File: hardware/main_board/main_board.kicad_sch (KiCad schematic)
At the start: 98 parts, among them J1 USB_C_Receptacle_USB2.0_16P, J2 BAT1, J3 Conn_02x05_Odd_Even, J4 Conn_02x05_Odd_Even, Q1 FDMC4435BZ, Q2 MMBT3904, Q3 MMBT3904, SW1 PTS645VK31LFS, SW2 PTS645VK31LFS, SW3 PTS645VK31LFS, U1 SRV05-4, U10 TPS61022, U11 ESP32-S3-WROOM1, U12 TPS2121, U13 TPS22810DBVR, U2 CP2102N-A02-GQFN28, U3 HUSB238_002DD, U4 TPS22918DBVR, U5 BQ25601, U6 DFPlayer_mini, U7 DS3231MZ, U8 TPS63802, U9 NCH2800HV

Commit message: WIP: mainboard pcb layout
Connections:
- net GND: no longer C3.2
- net PGND1: now also C3.2
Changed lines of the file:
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@@
 	)
 	(symbol
+		(lib_id "power:GNDPWR")
+		(at 80.01 39.37 0)
+		(unit 1)
+		(exclude_from_sim no)
+		(in_bom yes)
+		(on_board yes)
+		(dnp no)
+		(fields_autoplaced yes)
+		(property "Reference" "#PWR014"
+			(at 80.01 44.45 0)
+			(effects
+				(font
+					(size 1.27 1.27)
+				)
+				(hide yes)
+			)
+		)
+		(property "Value" "PGND1"
+			(at 79.883 43.18 0)
+			(effects
+				(font
+					(size 1.27 1.27)
+				)
+			)
+		)
+		(property "Footprint" ""
+			(at 80.01 40.64 0)
+			(effects
+				(font
+					(size 1.27 1.27)
+				)
+				(hide yes)
+			)
+		)
+		(property "Datasheet" ""
+			(at 80.01 40.64 0)
+			(effects
+				(font
+					(size 1.27 1.27)
+				)
+				(hide yes)
+			)
+		)
+		(property "Description" "Power symbol creates a global label with name \"GNDPWR\" , global ground"
+			(at 80.01 39.37 0)
+			(effects
+				(font
+					(size 1.27 1.27)
+				)
+				(hide yes)
+			)
+		)
+		(pin "1"
+		)
+		(instances
+			(project "main_board"
+				(path "/62950e93-3f98-4dee-9256-8213caa98ee7"
+					(reference "#PWR014")
+					(unit 1)
+				)
+			)
+		)
+	)
+	(symbol
 		(lib_id "Johnson_Symbol_Lib:TPS22918DBVR")
 		(at 128.27 226.06 0)
@@
 					(unit 1)
 				)
-			)
-		)
-	)
-	(symbol
-		(lib_id "power:GND")
-		(at 80.01 39.37 0)
-		(unit 1)
-		(exclude_from_sim no)
-		(in_bom yes)
-		(on_board yes)
-		(dnp no)
-		(fields_autoplaced yes)
-		(property "Reference" "#PWR014"
-			(at 80.01 45.72 0)
-			(effects
-				(font
-					(size 1.27 1.27)
-				)
-				(hide yes)
-			)
-		)
-		(property "Value" "GND"
-			(at 80.01 44.45 0)
-			(effects
-				(font
-					(size 1.27 1.27)
-				)
-			)
-		)
-		(property "Footprint" ""
-			(at 80.01 39.37 0)
-			(effects
-				(font
-					(size 1.27 1.27)
-				)
-				(hide yes)
-			)
-		)
-		(property "Datasheet" ""
-			(at 80.01 39.37 0)
-			(effects
-				(font
-					(size 1.27 1.27)
-				)
-				(hide yes)
-			)
-		)
-		(property "Description" "Power symbol creates a global label with name \"GND\" , ground"
-			(at 80.01 39.37 0)
-			(effects
-				(font
-					(size 1.27 1.27)
-				)
-				(hide yes)
-			)
-		)
-		(pin "1"
-		)
-		(instances
-			(project "main_board"
-				(path "/62950e93-3f98-4dee-9256-8213caa98ee7"
-					(reference "#PWR014")
-					(unit 1)
-				)

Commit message: WIP: update mainboard componemt LCSC PN
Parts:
- C16: LCSC PN (none) -> C23692981
- J2: footprint Connector_JST:JST_XH_S2B-XH-A_1x02_P2.50mm_Horizontal -> Connector_JST:JST_PH_B2B-PH-SM4-TB_1x02-1MP_P2.00mm_Vertical; LCSC PN C240819 -> C3029431
- LS1: footprint Connector_JST:JST_XH_S2B-XH-A_1x02_P2.50mm_Horizontal -> Connector_JST:JST_PH_B2B-PH-SM4-TB_1x02-1MP_P2.00mm_Vertical; LCSC PN C19270574 -> (none)
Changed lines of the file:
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@@
 			)
 		)
-		(property "Footprint" "Connector_JST:JST_XH_S2B-XH-A_1x02_P2.50mm_Horizontal"
+		(property "Footprint" "Connector_JST:JST_PH_B2B-PH-SM4-TB_1x02-1MP_P2.00mm_Vertical"
 			(at 144.78 237.49 0)
 			(effects
@@
 			)
 		)
-		(property "LCSC PN" "C19270574"
+		(property "LCSC PN" ""
 			(at 144.78 242.57 0)
 			(effects
@@
 			)
 		)
-		(property "Footprint" "Connector_JST:JST_XH_S2B-XH-A_1x02_P2.50mm_Horizontal"
+		(property "Footprint" "Connector_JST:JST_PH_B2B-PH-SM4-TB_1x02-1MP_P2.00mm_Vertical"
 			(at 167.64 88.9 0)
 			(effects
@@
 			)
 		)
-		(property "LCSC PN" "C240819"
+		(property "LCSC PN" "C3029431"
 			(at 167.64 88.9 0)
 			(effects
@@
 			(at 274.32 43.18 0)
 			(effects
+				(font
+					(size 1.27 1.27)
+				)
+				(hide yes)
+			)
+		)
+		(property "LCSC PN" "C23692981"
+			(at 274.32 43.18 0)
+			(effects

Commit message: WIP: update component LCSCPN
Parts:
- J2, LS1: now in the parts list
- R29: LCSC PN (none) -> C102991
- R7: LCSC PN (none) -> C25077
- R73: LCSC PN (none) -> C21189
- U10: LCSC PN (none) -> C2071784
- U8: LCSC PN (none) -> C2845237
- U9: now left out of the parts list
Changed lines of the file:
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@@
 			)
 		)
-		(property "LCSC PN" ""
+		(property "LCSC PN" "C21189"
 			(at 256.54 201.93 90)
 			(effects
@@
 		(unit 1)
 		(exclude_from_sim no)
-		(in_bom yes)
+		(in_bom no)
 		(on_board yes)
 		(dnp no)
@@
 		(unit 1)
 		(exclude_from_sim no)
-		(in_bom no)
+		(in_bom yes)
 		(on_board yes)
 		(dnp no)
@@
 		(unit 1)
 		(exclude_from_sim no)
-		(in_bom no)
+		(in_bom yes)
 		(on_board yes)
 		(dnp no)
@@
 			)
 		)
+		(property "LCSC PN" "C2845237"
+			(at 245.11 41.91 0)
+			(effects
+				(font
+					(size 1.27 1.27)
+				)
+				(hide yes)
+			)
+		)
 		(pin "9"
 		)
@@
 			)
 		)
+		(property "LCSC PN" "C2071784"
+			(at 278.13 80.01 0)
+			(effects
+				(font
+					(size 1.27 1.27)
+				)
+				(hide yes)
+			)
+		)
 		(pin "4"
 		)
@@
 			)
 		)
+		(property "LCSC PN" "C102991"
+			(at 309.88 25.4 0)
+			(effects
+				(font
+					(size 1.27 1.27)
+				)
+				(hide yes)
+			)
+		)
 		(pin "1"
 		)
@@
 			)
 		)
-		(property "LCSC PN" ""
+		(property "LCSC PN" "C25077"
 			(at 111.76 38.1 90)
 			(effects

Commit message: WIP: mainboard schematic
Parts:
- R18: LCSC PN C11616 -> C100463
- SW1, SW2, SW3: now left out of the parts list
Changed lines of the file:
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@@
 		(unit 1)
 		(exclude_from_sim no)
-		(in_bom yes)
+		(in_bom no)
 		(on_board yes)
 		(dnp no)
@@
 		(unit 1)
 		(exclude_from_sim no)
-		(in_bom yes)
+		(in_bom no)
 		(on_board yes)
 		(dnp no)
@@
 			)
 		)
-		(property "LCSC PN" "C11616"
+		(property "LCSC PN" "C100463"
 			(at 265.43 38.1 0)
 			(effects
@@
 		(unit 1)
 		(exclude_from_sim no)
-		(in_bom yes)
+		(in_bom no)
 		(on_board yes)
 		(dnp no)

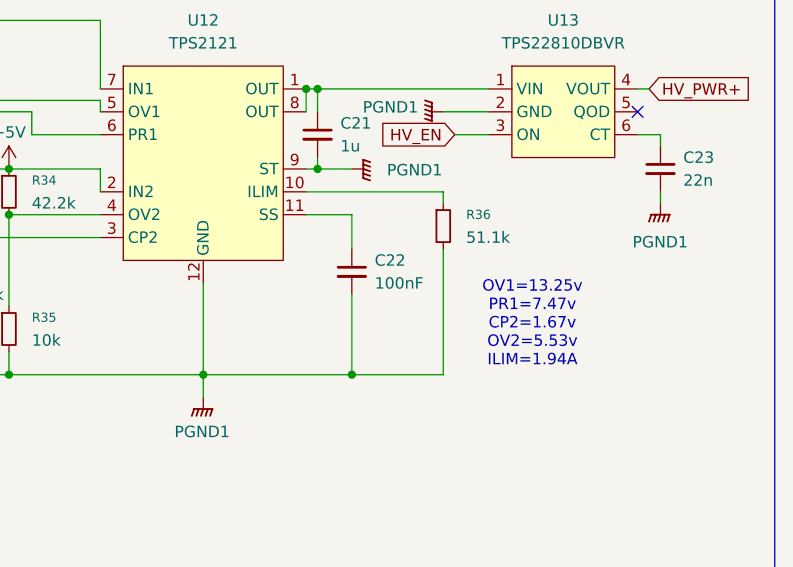
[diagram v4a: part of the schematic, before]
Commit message: hw(main_board): update LCSC PN
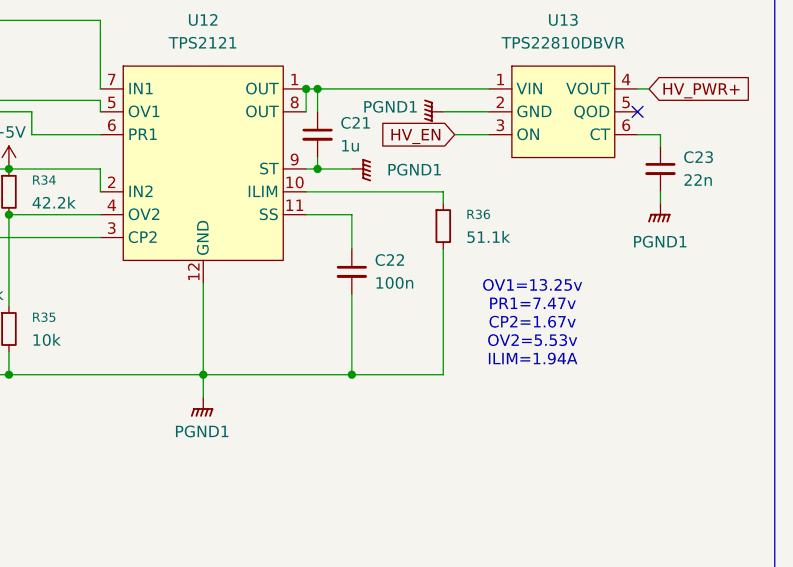
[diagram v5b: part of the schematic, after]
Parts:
- C22: value 100nF -> 100n
- LS1: LCSC PN (none) -> C3029431
- R19: LCSC PN C4147 -> C284722
- R2: LCSC PN C25896 -> C103064
- R27, R30, R32, R35: LCSC PN C25804 -> C98220
- R29: LCSC PN C102991 -> C23141
- R6: LCSC PN C22855 -> C25850
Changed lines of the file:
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@@
 			)
 		)
-		(property "LCSC PN" ""
+		(property "LCSC PN" "C3029431"
 			(at 144.78 242.57 0)
 			(effects
@@
 			)
 		)
-		(property "LCSC PN" "C22855"
+		(property "LCSC PN" "C25850"
 			(at 105.41 63.5 90)
 			(effects
@@
 			)
 		)
-		(property "LCSC PN" "C25804"
+		(property "LCSC PN" "C98220"
 			(at 316.23 50.8 0)
 			(effects
@@
 			)
 		)
-		(property "LCSC PN" "C25804"
+		(property "LCSC PN" "C98220"
 			(at 300.99 36.83 0)
 			(effects
@@
 			)
 		)
-		(property "LCSC PN" "C25896"
+		(property "LCSC PN" "C103064"
 			(at 26.67 125.73 0)
 			(effects
@@
 			)
 		)
-		(property "LCSC PN" "C25804"
+		(property "LCSC PN" "C98220"
 			(at 309.88 36.83 0)
 			(effects
@@
 			)
 		)
-		(property "LCSC PN" "C4147"
+		(property "LCSC PN" "C284722"
 			(at 265.43 48.26 0)
 			(effects
@@
 			)
 		)
-		(property "LCSC PN" "C25804"
+		(property "LCSC PN" "C98220"
 			(at 322.58 55.88 0)
 			(effects
@@
 			)
 		)
-		(property "LCSC PN" "C102991"
+		(property "LCSC PN" "C23141"
 			(at 309.88 25.4 0)
 			(effects
@@
 			)
 		)
-		(property "Value" "100nF"
+		(property "Value" "100n"
 			(at 363.22 50.8062 0)
 			(effects

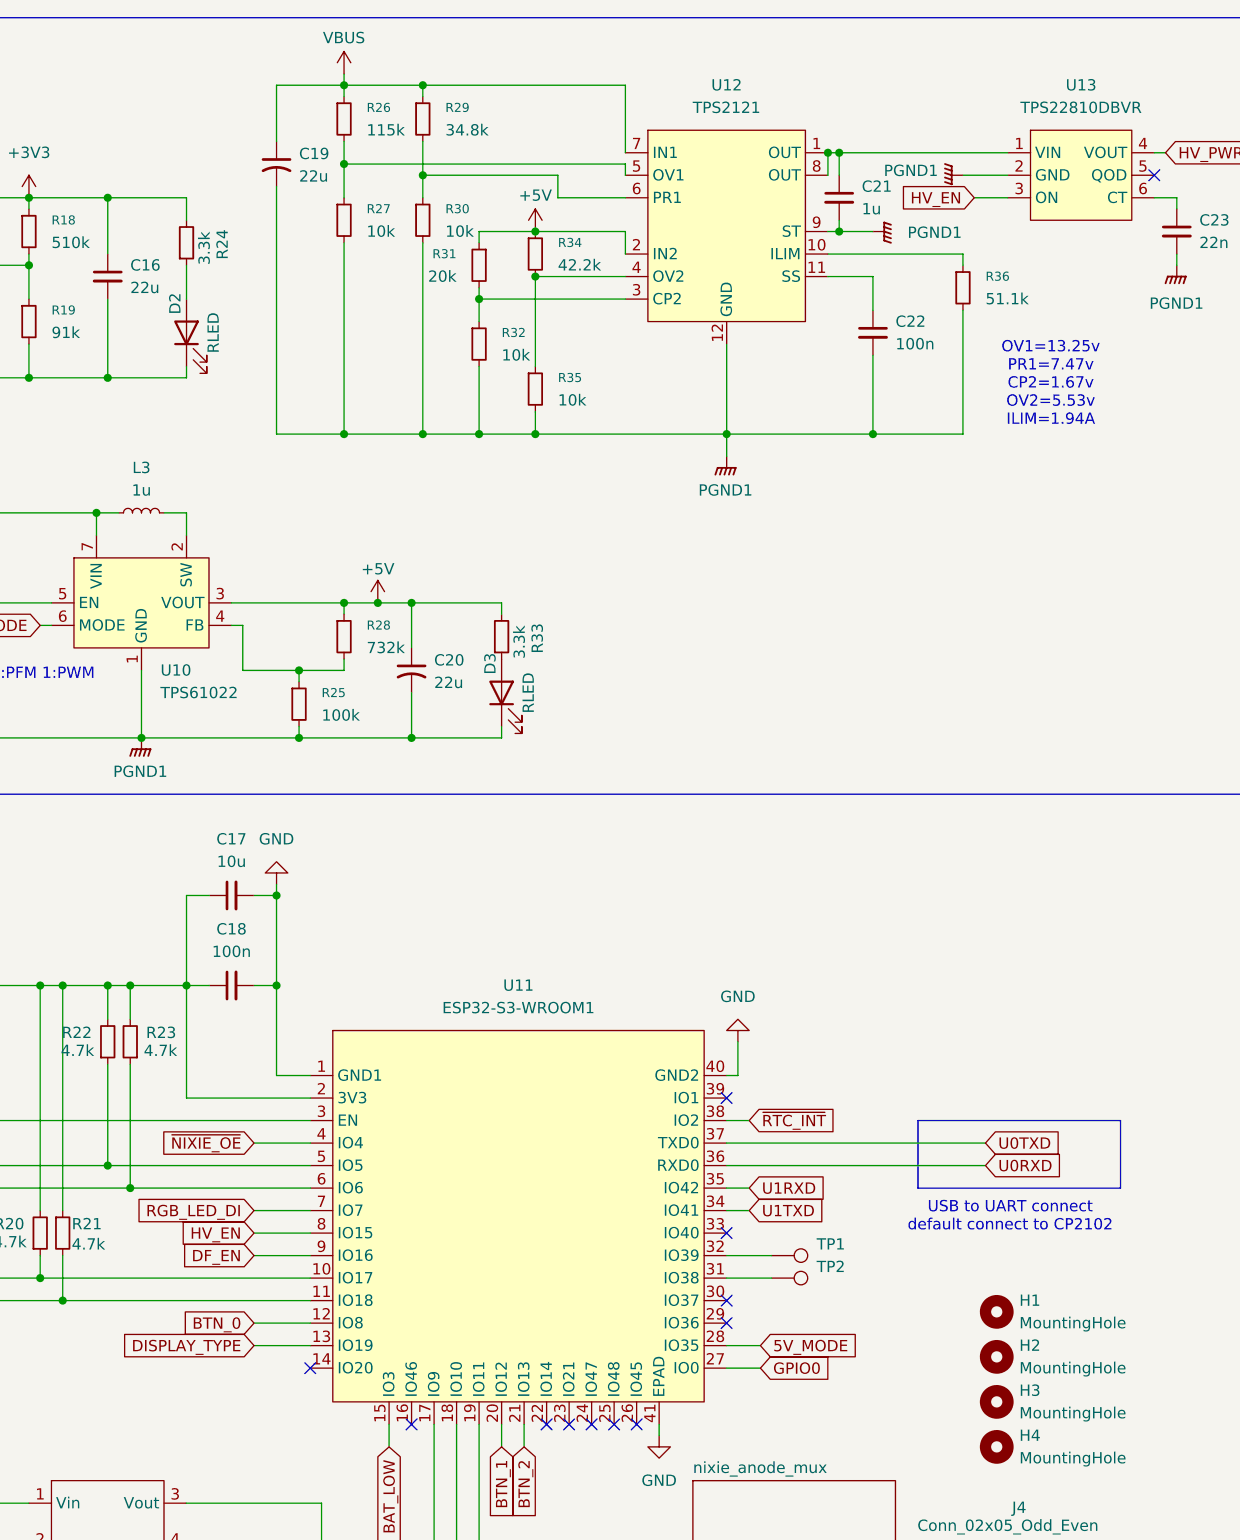
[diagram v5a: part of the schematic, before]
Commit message: hw(sch): add input detect signal from TPS2121 to let ESP32 know which input is selected for HV power
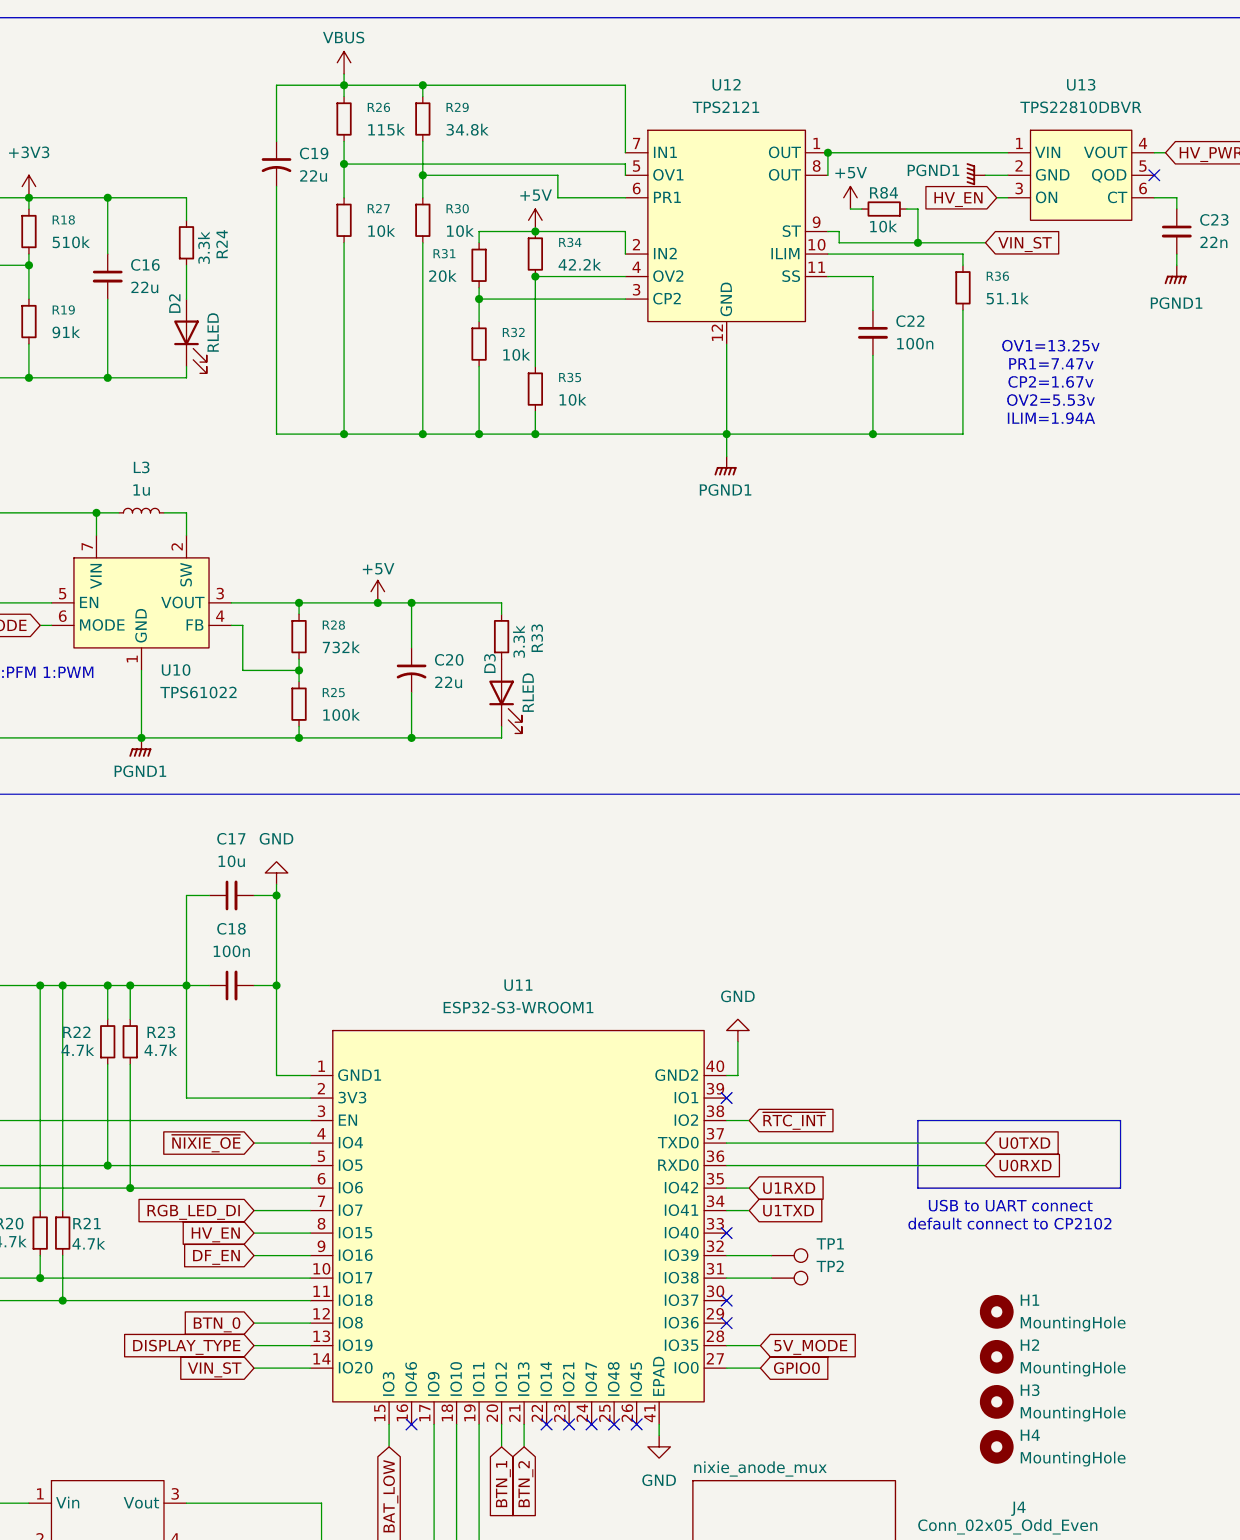
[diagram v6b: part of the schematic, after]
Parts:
- removed C21: 1u, Capacitor_SMD:C_0603_1608Metric, symbol Device:C_Small
- added R84: 10k, Resistor_SMD:R_0402_1005Metric, symbol Device:R_Small
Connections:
- net +5V: now also R84.2
- net PGND1: no longer U12.9 (ST)
- net VIN_ST: now reaches U11.14 (IO20)
- net VIN_ST: now also U12.9 (ST), R84.1
- no-connect marks 47 -> 46
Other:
- moved on the sheet: R28

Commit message: layout(main): change battery and speaker connector footprint
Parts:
- J2, LS1: footprint Connector_JST:JST_PH_B2B-PH-SM4-TB_1x02-1MP_P2.00mm_Vertical -> Connector_JST:JST_PH_S2B-PH-SM4-TB_1x02-1MP_P2.00mm_Horizontal; LCSC PN C3029431 -> C3029440
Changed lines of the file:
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@@
 			)
 		)
-		(property "Footprint" "Connector_JST:JST_PH_B2B-PH-SM4-TB_1x02-1MP_P2.00mm_Vertical"
+		(property "Footprint" "Connector_JST:JST_PH_S2B-PH-SM4-TB_1x02-1MP_P2.00mm_Horizontal"
 			(at 144.78 237.49 0)
 			(effects
@@
 			)
 		)
-		(property "LCSC PN" "C3029431"
+		(property "LCSC PN" "C3029440"
 			(at 144.78 242.57 0)
 			(effects
@@
 			)
 		)
-		(property "Footprint" "Connector_JST:JST_PH_B2B-PH-SM4-TB_1x02-1MP_P2.00mm_Vertical"
+		(property "Footprint" "Connector_JST:JST_PH_S2B-PH-SM4-TB_1x02-1MP_P2.00mm_Horizontal"
 			(at 167.64 88.9 0)
 			(effects
@@
 			)
 		)
-		(property "LCSC PN" "C3029431"
+		(property "LCSC PN" "C3029440"
 			(at 167.64 88.9 0)
 			(effects
